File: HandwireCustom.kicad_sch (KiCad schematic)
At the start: 28 parts, among them J1 ICSP, J2 Conn_01x04, SW1 SW_Push, U1 ATmega32U4RC-M, Y1 16Mhz 9pF

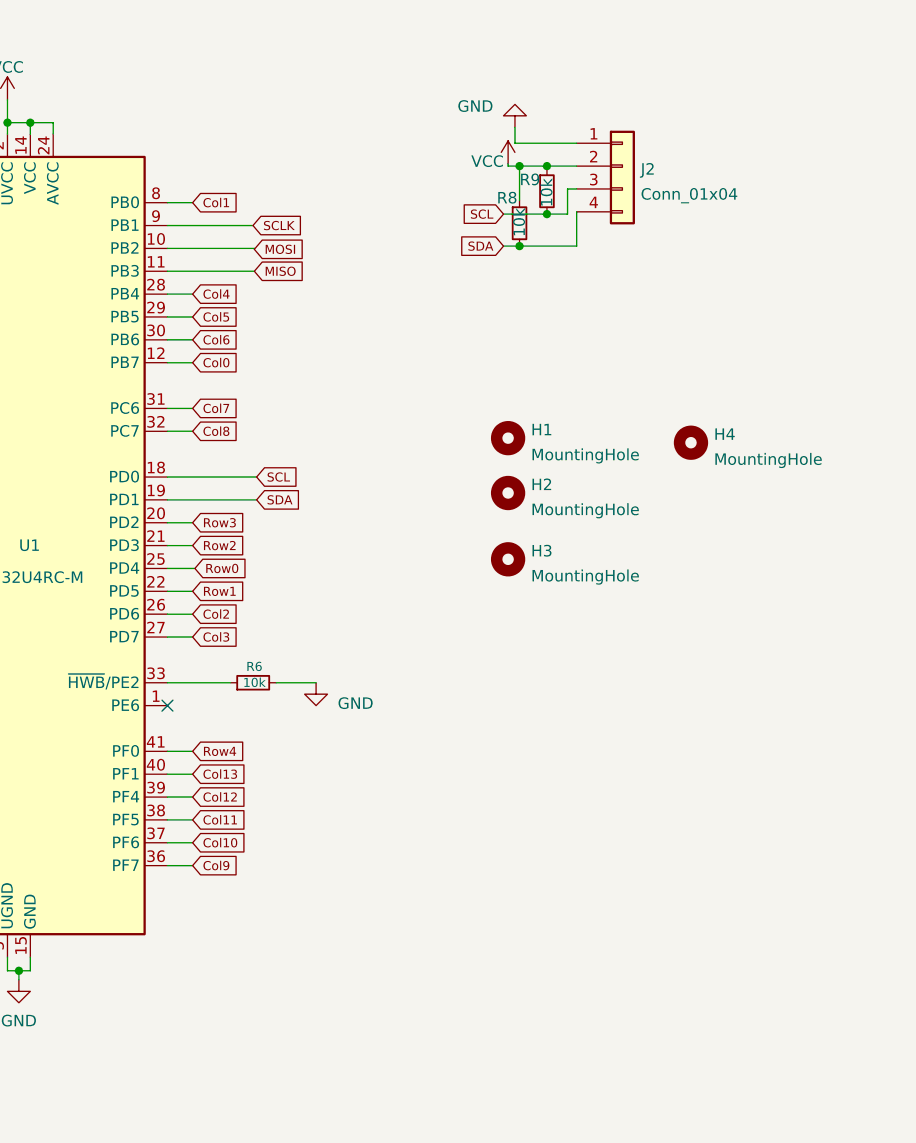
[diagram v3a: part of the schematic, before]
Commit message: Rerouted, new parts
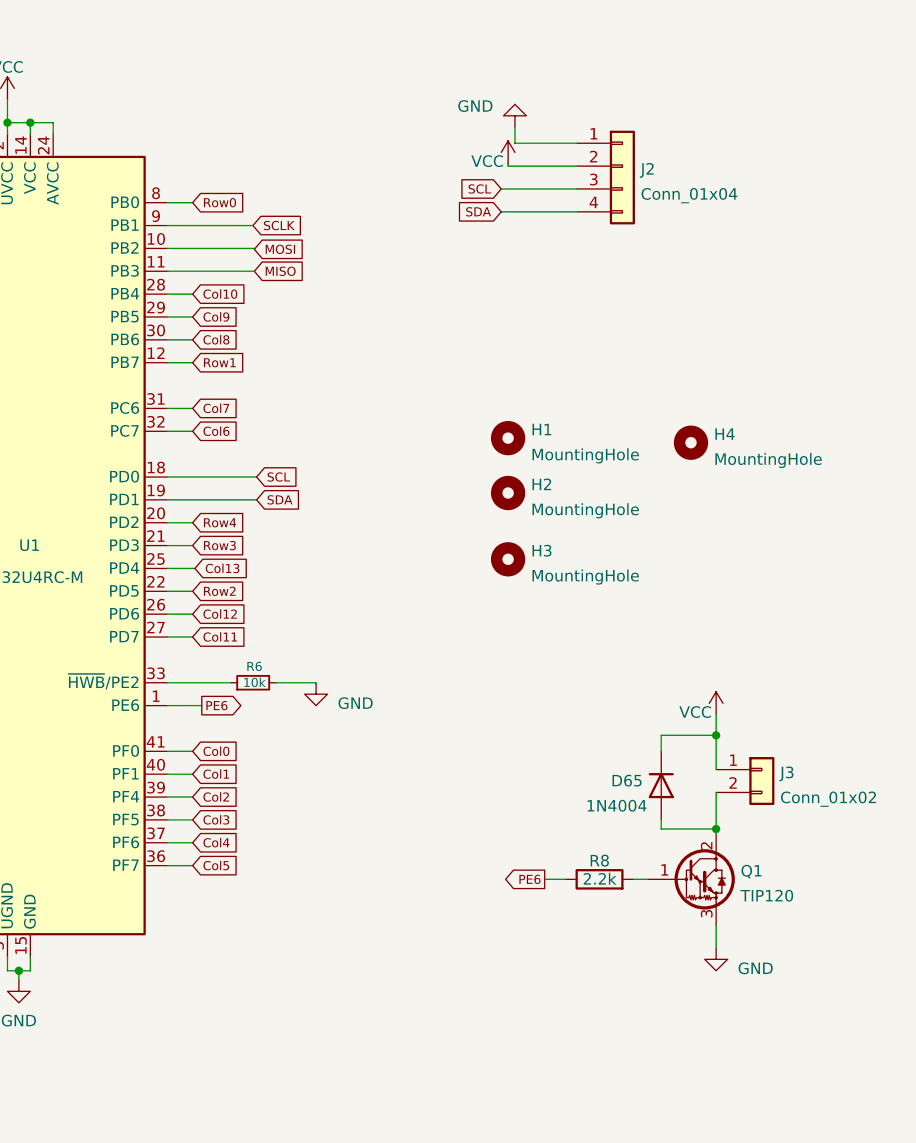
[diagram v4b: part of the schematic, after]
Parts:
- removed R8, R9: 10k, Resistor_SMD:R_0402_1005Metric, symbol Device:R_Small
- added D65: 1N4004, Diode_SMD:D_SMA, symbol Diode:1N4004
- added J3: Conn_01x02, Connector_PinHeader_2.54mm:PinHeader_1x02_P2.54mm_Vertical, symbol Connector_Generic:Conn_01x02
- added Q1: TIP120, Package_TO_SOT_THT:TO-220-3_Vertical, symbol Transistor_BJT:TIP120
- added R8: 2.2k, Resistor_SMD:R_0603_1608Metric, symbol Device:R
- R5, R7: footprint Resistor_THT:R_Axial_DIN0204_L3.6mm_D1.6mm_P5.08mm_Horizontal -> Resistor_SMD:R_0402_1005Metric
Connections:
- net Col0: now also U1.41 (PF0); no longer U1.12 (PB7)
- net Col1: now also U1.40 (PF1); no longer U1.8 (PB0)
- net Col10: now also U1.28 (PB4); no longer U1.37 (PF6)
- net Col11: now also U1.27 (PD7); no longer U1.38 (PF5)
- net Col12: now also U1.26 (PD6); no longer U1.39 (PF4)
- net Col13: now also U1.25 (PD4); no longer U1.40 (PF1)
- net Col2: now also U1.39 (PF4); no longer U1.26 (PD6)
- net Col3: now also U1.38 (PF5); no longer U1.27 (PD7)
- net Col4: now also U1.37 (PF6); no longer U1.28 (PB4)
- net Col5: now also U1.36 (PF7); no longer U1.29 (PB5)
- net Col6: now also U1.32 (PC7); no longer U1.30 (PB6)
- net Col8: now also U1.30 (PB6); no longer U1.32 (PC7)
- net Col9: now also U1.29 (PB5); no longer U1.36 (PF7)
- net GND: now also Q1.3 (E)
- net Row0: now also U1.8 (PB0); no longer U1.25 (PD4)
- net Row1: now also U1.12 (PB7); no longer U1.22 (PD5)
- net Row2: now also U1.22 (PD5); no longer U1.21 (PD3)
- net Row3: now also U1.21 (PD3); no longer U1.20 (PD2)
- net Row4: now also U1.20 (PD2); no longer U1.41 (PF0)
- net VCC: now also D65.1 (K), J3.1 (Pin_1)
- net PE6: now reaches U1.1 (PE6)
- net PE6: now also R8.1
- new net: D65.2 (A), J3.2 (Pin_2), Q1.2 (C)
- new net: Q1.1 (B), R8.2
- no-connect marks 4 -> 3

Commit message: Ready for JLCPCB
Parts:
- C1, C2: LCSC (none) -> C1547
- C3: LCSC (none) -> C19666
- C4, C5, C6, C7: LCSC (none) -> C1525
- C8: LCSC (none) -> C52923
- D65: value 1N4004 -> 1N4001; LCSC (none) -> C727079
- R1, R2: LCSC (none) -> C25905
- R3, R4: LCSC (none) -> C25092
- R5, R6: LCSC (none) -> C25744
- R7: LCSC (none) -> C25091
- R8: LCSC (none) -> C4190
- U1: LCSC (none) -> C112161
- USB1: LCSC (none) -> C165948
- Y1: LCSC (none) -> C13738
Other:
- moved on the sheet: H2, H4
